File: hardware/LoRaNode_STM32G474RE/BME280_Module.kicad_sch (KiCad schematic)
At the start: 2 parts

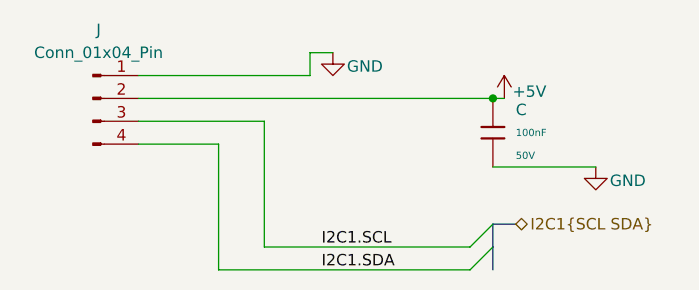
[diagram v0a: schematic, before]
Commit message: feat: add RFM95W 3D model for hardware and initial FreeRTOS task skeleton for firmware
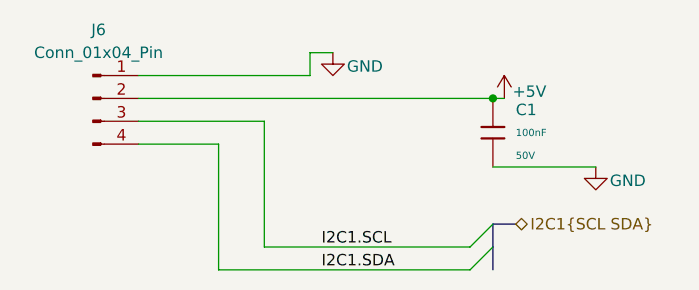
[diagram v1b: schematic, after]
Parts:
- renumbered C to C1, J to J6
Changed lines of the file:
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@@
 		(dnp no)
 		(fields_autoplaced yes)
-		(property "Reference" "C"
+		(property "Reference" "C1"
 			(at 165.1 88.8999 0)
 			(effects
@@
 		(pin "2"
 		)
-		(instances)
+		(instances
+			(project "LoRaNode_STM32G474RE"
+				(path "/f7616d52-da00-4113-a545-55bdab5f2510/b05dcf68-9f66-4f64-bb1b-2c38b09db937"
+					(reference "C1")
+					(unit 1)
+				)
+			)
+		)
 	)
 	(symbol
@@
 		(on_board yes)
 		(dnp no)
-		(property "Reference" "#PWR"
+		(property "Reference" "#PWR04"
 			(at 173.99 101.6 0)
 			(effects
@@
 		(pin "1"
 		)
-		(instances)
+		(instances
+			(project "LoRaNode_STM32G474RE"
+				(path "/f7616d52-da00-4113-a545-55bdab5f2510/b05dcf68-9f66-4f64-bb1b-2c38b09db937"
+					(reference "#PWR04")
+					(unit 1)
+				)
+			)
+		)
 	)
 	(symbol
@@
 		(on_board yes)
 		(dnp no)
-		(property "Reference" "#PWR"
+		(property "Reference" "#PWR03"
 			(at 163.83 91.44 0)
 			(effects
@@
 		(pin "1"
 		)
-		(instances)
+		(instances
+			(project "LoRaNode_STM32G474RE"
+				(path "/f7616d52-da00-4113-a545-55bdab5f2510/b05dcf68-9f66-4f64-bb1b-2c38b09db937"
+					(reference "#PWR03")
+					(unit 1)
+				)
+			)
+		)
 	)
 	(symbol
@@
 		(dnp no)
 		(fields_autoplaced yes)
-		(property "Reference" "J"
+		(property "Reference" "J6"
 			(at 118.745 80.01 0)
 			(effects
@@
 		(pin "2"
 		)
-		(instances)
+		(instances
+			(project "LoRaNode_STM32G474RE"
+				(path "/f7616d52-da00-4113-a545-55bdab5f2510/b05dcf68-9f66-4f64-bb1b-2c38b09db937"
+					(reference "J6")
+					(unit 1)
+				)
+			)
+		)
 	)
 	(symbol
@@
 		(on_board yes)
 		(dnp no)
-		(property "Reference" "#PWR"
+		(property "Reference" "#PWR02"
 			(at 144.78 88.9 0)
 			(effects
@@
 		(pin "1"
 		)
-		(instances)
+		(instances
+			(project "LoRaNode_STM32G474RE"
+				(path "/f7616d52-da00-4113-a545-55bdab5f2510/b05dcf68-9f66-4f64-bb1b-2c38b09db937"
+					(reference "#PWR02")
+					(unit 1)
+				)
+			)
+		)
 	)
 )
